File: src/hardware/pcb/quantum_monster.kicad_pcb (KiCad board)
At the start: 2 copper layers, 50.9 x 39.9 mm, 28 parts, among them J1 ICSP, J2 PCD8544, Q1 VS1838B, SW1 RESET, SW2 A, SW3 B, SW4 C, U1 ATmega328P-PU, Y1 32.768kHz

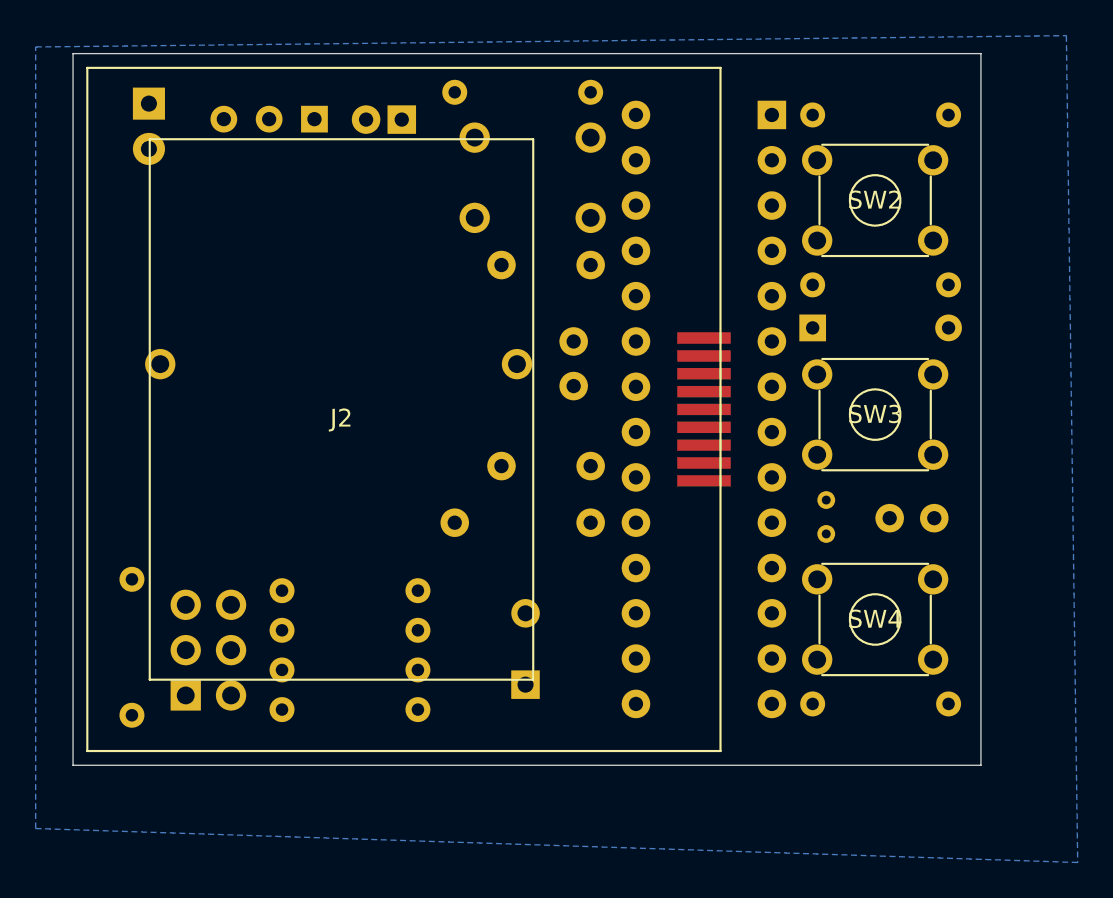
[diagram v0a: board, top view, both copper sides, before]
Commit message: Begin layout changes to accommodate correct display dimensions.
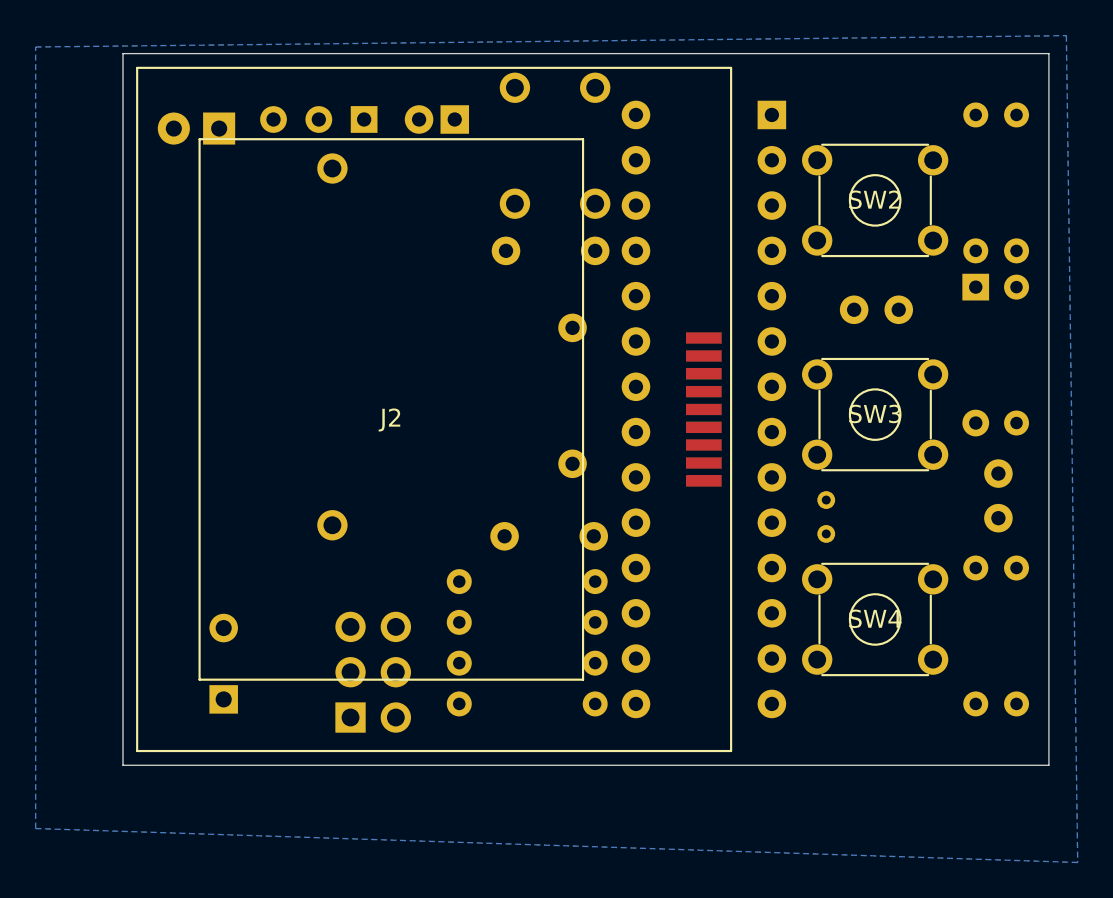
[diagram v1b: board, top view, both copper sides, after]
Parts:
- moved R8 49.6 mm to (140.7, 104.1)
- moved R9 29.2 mm to (138.4, 78.7), turned to 270 degrees
- moved BZ1 16.9 mm to (96.3, 111.5)
- moved C2 16.3 mm to (131.6, 89.7), turned to 0 degrees
- moved L1 12.8 mm to (115.8, 90.7), turned to 270 degrees
- moved R6 9.95 mm to (117.1, 104.9)
- moved R5 9.95 mm to (117.1, 107.2)
- moved R3 9.95 mm to (109.5, 109.5)
- moved R4 9.94 mm to (109.5, 111.8)
- moved D1 9.43 mm to (138.4, 88.4), turned to 270 degrees
- moved J1 9.32 mm to (103.4, 112.5)
- moved R7 7.77 mm to (138.4, 104.1), turned to 270 degrees
- moved SW1 7.63 mm to (112.6, 77.2), turned to 270 degrees
- moved C1 4.38 mm to (139.7, 98.8), turned to 270 degrees
- moved D2 4.18 mm to (96.0, 79.5), turned to 180 degrees
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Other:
- board size 50.9 x 39.9 mm -> 51.9 x 39.9 mm

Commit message: Upgrade to KiCad 6.
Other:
- net class Default removed

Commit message: Initial production prototype of PCB.
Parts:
- moved D1 13.7 mm to (138.4, 102.1), turned to 90 degrees
- moved SW1 9.20 mm to (117.1, 85.2), turned to 90 degrees
- moved C1 9.18 mm to (139.6, 89.7), turned to 180 degrees
- moved R9 9.02 mm to (129.4, 78.7), turned to 0 degrees
- moved R3 8.81 mm to (117.2, 105.3), turned to 180 degrees
- moved R7 7.75 mm to (137.0, 111.8), turned to 180 degrees
- moved R8 7.69 mm to (139.7, 111.8), turned to 90 degrees
- moved R6 6.86 mm to (117.2, 111.8)
- moved R1 6.10 mm to (140.6, 94.5)
- moved R4 4.32 mm to (109.6, 107.4)
- moved R5 2.42 mm to (117.2, 109.6)
- moved R2 1.52 mm to (139.2, 78.7)
- moved C4 1.27 mm to (117.1, 87.6)
- moved C2 0.80 mm to (130.8, 89.7)
- moved D2 0.64 mm to (96.6, 79.5)
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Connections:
- net DISPLAY_CLOCK renamed DISPLAY_SCLK
- net DISPLAY_MOSI renamed DISPLAY_SDIN
- J1 pad 2: Net-(J1-Pad2) -> unconnected-(J1-Pad2)
- J2 pad 1: DISPLAY_RESET -> DISPLAY_RES
- J2 pad 6: DISPLAY_DATA_COMMAND -> DISPLAY_DC
- Q1 pad 3: LINK_RECEIVER_DATA -> INFRARED_RECEIVER_OUT
- R8 pad 2: LINK_TRANSMITTER -> INFRARED_TRANSMITTER
- R9 pad 2: LINK_RECEIVER_POWER -> INFRARED_RECEIVER_POWER
- SW2 pad 1: GND -> A_BUTTON
- SW2 pad 2: A_BUTTON -> GND
- U1 pad 11: DISPLAY_DATA_COMMAND -> B_BUTTON
- U1 pad 12: SPEAKER -> INFRARED_TRANSMITTER
- U1 pad 13: Net-(U1-Pad13) -> C_BUTTON
- U1 pad 14: Net-(U1-Pad14) -> unconnected-(U1-Pad14)
- U1 pad 15: LINK_TRANSMITTER -> SPEAKER
- U1 pad 16: Net-(U1-Pad16) -> unconnected-(U1-Pad16)
- U1 pad 2: Net-(U1-Pad2) -> A_BUTTON
- U1 pad 21: Net-(U1-Pad21) -> unconnected-(U1-Pad21)
- U1 pad 23: Net-(U1-Pad23) -> DISPLAY_RES
- U1 pad 24: DISPLAY_RESET -> DISPLAY_DC
- U1 pad 25: C_BUTTON -> unconnected-(U1-Pad25)
- U1 pad 26: Net-(U1-Pad26) -> unconnected-(U1-Pad26)
- U1 pad 27: LINK_RECEIVER_DATA -> unconnected-(U1-Pad27)
- U1 pad 28: LINK_RECEIVER_POWER -> INFRARED_RECEIVER_OUT
- U1 pad 4: Net-(U1-Pad4) -> INFRARED_RECEIVER_POWER
- U1 pad 5: Net-(U1-Pad5) -> unconnected-(U1-Pad5)
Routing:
- net Net-(D2-Pad2): track 0.00 -> 79.8 mm
- net RESET: track 0.00 -> 78.9 mm
- net VCC: track 0.00 -> 74.7 mm
- net Net-(BZ1-Pad1): track 0.00 -> 42.5 mm
- net Net-(C5-Pad1): track 0.00 -> 27.0 mm
- net Net-(R2-Pad2): track 0.00 -> 24.7 mm
- net INFRARED_RECEIVER_POWER: track 0.00 -> 23.3 mm
- net MISO: track 0.00 -> 20.9 mm
- net INFRARED_RECEIVER_OUT: track 0.00 -> 20.8 mm
- net FILTERED_VCC: track 0.00 -> 19.5 mm
- net B_BUTTON: track 0.00 -> 16.2 mm
- net DISPLAY_SDIN: track 0.00 -> 15.7 mm
- net INFRARED_TRANSMITTER: track 0.00 -> 13.8 mm
- net DISPLAY_DC: track 0.00 -> 13.1 mm
- net C_BUTTON: track 0.00 -> 12.1 mm
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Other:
- board text added: "GND"
- board text added: "MISO"
- board text added: "MOSI"
- board text added: "NC"
- board text added: "RST"
- board text added: "SCK"
